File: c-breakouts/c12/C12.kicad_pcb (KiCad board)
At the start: 2 copper layers, 38.1 x 48.3 mm, 54 parts, among them J1 Conn_01x10_Female, J10 Conn_01x01_Male, J11 Conn_01x01_Male, J2 Conn_01x10_Female, J3 Conn_01x10_Female, J4 Conn_01x10_Female, J5 Conn_01x10_Female, J6 Conn_01x10_Female

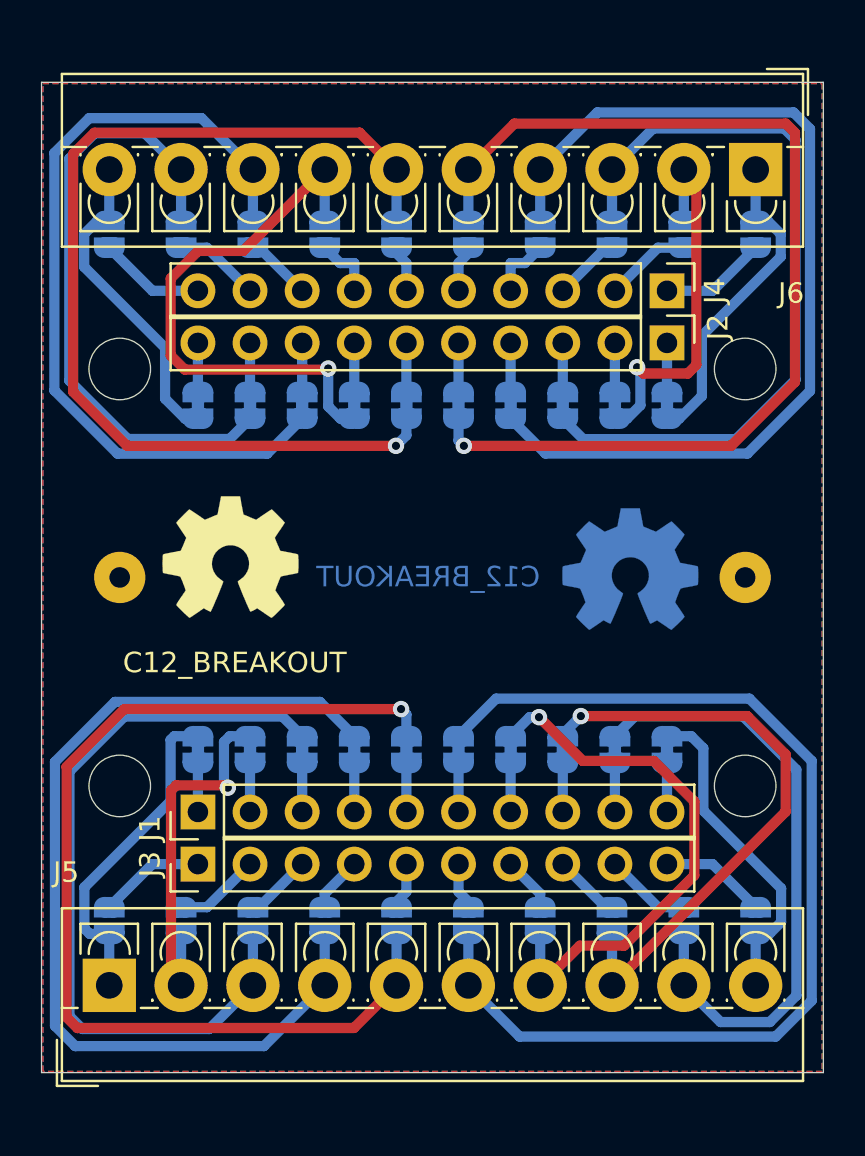
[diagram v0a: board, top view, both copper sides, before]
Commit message: fixed C12 connector position
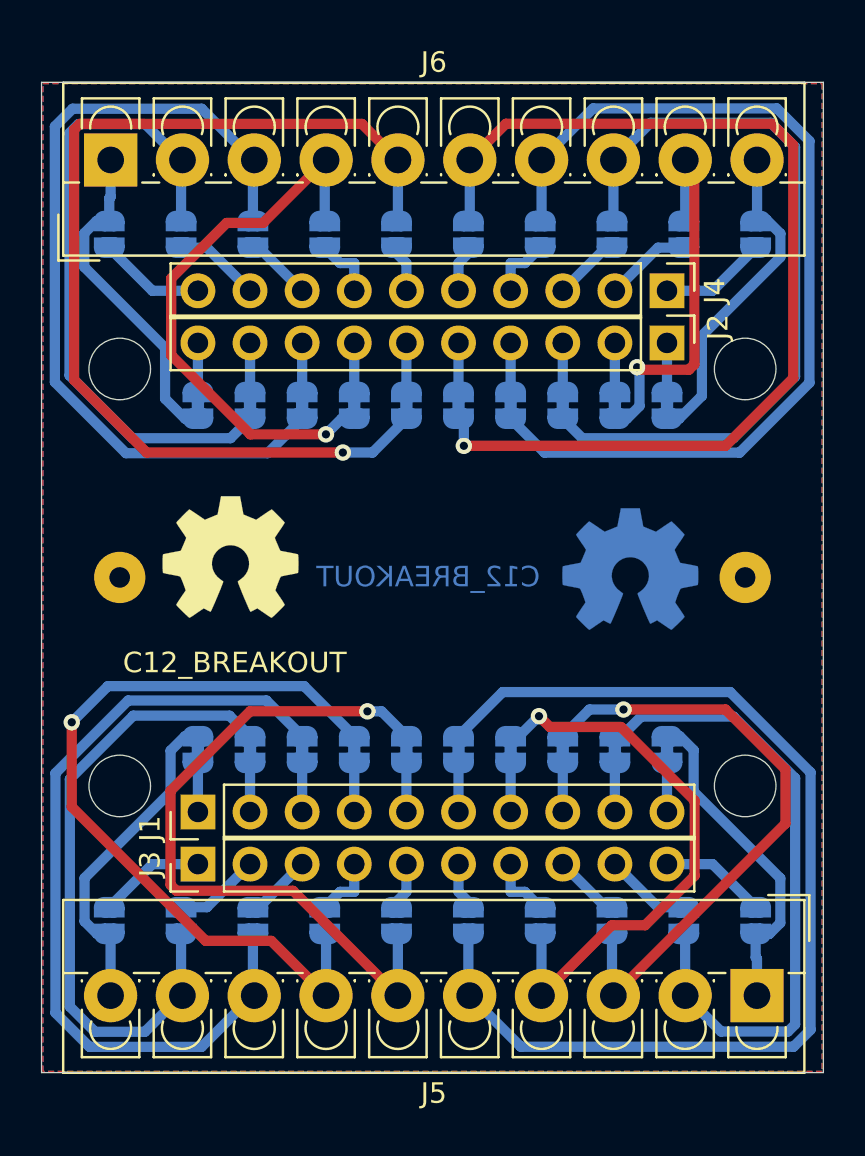
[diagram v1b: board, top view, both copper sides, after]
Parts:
- moved J5 31.6 mm to (54.9, 64.5), turned to 180 degrees
- moved J6 31.4 mm to (23.4, 23.8), turned to 0 degrees
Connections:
- J5 pad 1: Net-(J5-Pad1) -> Net-(JP10-Pad1)
- J5 pad 10: Net-(J5-Pad10) -> Net-(JP1-Pad1)
- J5 pad 2: Net-(J5-Pad2) -> Net-(JP19-Pad1)
- J5 pad 3: Net-(J5-Pad3) -> Net-(JP18-Pad1)
- J5 pad 4: Net-(J5-Pad4) -> Net-(JP17-Pad1)
- J5 pad 5: Net-(J5-Pad5) -> Net-(JP16-Pad1)
- J5 pad 6: Net-(J5-Pad6) -> Net-(JP15-Pad1)
- J5 pad 7: Net-(J5-Pad7) -> Net-(JP14-Pad1)
- J5 pad 8: Net-(J5-Pad8) -> Net-(JP13-Pad1)
- J5 pad 9: Net-(J5-Pad9) -> Net-(JP12-Pad1)
- J6 pad 1: Net-(J6-Pad1) -> Net-(JP30-Pad2)
- J6 pad 10: Net-(J6-Pad10) -> Net-(JP21-Pad2)
- J6 pad 2: Net-(J6-Pad2) -> Net-(JP29-Pad2)
- J6 pad 3: Net-(J6-Pad3) -> Net-(JP28-Pad2)
- J6 pad 4: Net-(J6-Pad4) -> Net-(JP27-Pad2)
- J6 pad 5: Net-(J6-Pad5) -> Net-(JP26-Pad2)
- J6 pad 6: Net-(J6-Pad6) -> Net-(JP25-Pad2)
- J6 pad 7: Net-(J6-Pad7) -> Net-(JP24-Pad2)
- J6 pad 8: Net-(J6-Pad8) -> Net-(JP23-Pad2)
- J6 pad 9: Net-(J6-Pad9) -> Net-(JP22-Pad2)
- JP1 pad 1: Net-(J5-Pad1) -> Net-(JP1-Pad1)
- JP10 pad 1: Net-(J5-Pad10) -> Net-(JP10-Pad1)
- JP11 pad 1: Net-(J5-Pad1) -> Net-(JP1-Pad1)
- JP12 pad 1: Net-(J5-Pad2) -> Net-(JP12-Pad1)
- JP13 pad 1: Net-(J5-Pad3) -> Net-(JP13-Pad1)
- JP14 pad 1: Net-(J5-Pad4) -> Net-(JP14-Pad1)
- JP15 pad 1: Net-(J5-Pad5) -> Net-(JP15-Pad1)
- JP16 pad 1: Net-(J5-Pad6) -> Net-(JP16-Pad1)
- JP17 pad 1: Net-(J5-Pad7) -> Net-(JP17-Pad1)
- JP18 pad 1: Net-(J5-Pad8) -> Net-(JP18-Pad1)
- JP19 pad 1: Net-(J5-Pad9) -> Net-(JP19-Pad1)
- JP2 pad 1: Net-(J5-Pad2) -> Net-(JP12-Pad1)
- JP20 pad 1: Net-(J5-Pad10) -> Net-(JP10-Pad1)
- JP21 pad 2: Net-(J6-Pad1) -> Net-(JP21-Pad2)
- JP22 pad 2: Net-(J6-Pad2) -> Net-(JP22-Pad2)
- JP23 pad 2: Net-(J6-Pad3) -> Net-(JP23-Pad2)
- JP24 pad 2: Net-(J6-Pad4) -> Net-(JP24-Pad2)
- JP25 pad 2: Net-(J6-Pad5) -> Net-(JP25-Pad2)
- JP26 pad 2: Net-(J6-Pad6) -> Net-(JP26-Pad2)
- JP27 pad 2: Net-(J6-Pad7) -> Net-(JP27-Pad2)
- JP28 pad 2: Net-(J6-Pad8) -> Net-(JP28-Pad2)
- JP29 pad 2: Net-(J6-Pad9) -> Net-(JP29-Pad2)
- JP3 pad 1: Net-(J5-Pad3) -> Net-(JP13-Pad1)
- JP30 pad 2: Net-(J6-Pad10) -> Net-(JP30-Pad2)
- JP31 pad 2: Net-(J6-Pad1) -> Net-(JP21-Pad2)
- JP32 pad 2: Net-(J6-Pad2) -> Net-(JP22-Pad2)
- JP33 pad 2: Net-(J6-Pad3) -> Net-(JP23-Pad2)
- JP34 pad 2: Net-(J6-Pad4) -> Net-(JP24-Pad2)
- JP35 pad 2: Net-(J6-Pad5) -> Net-(JP25-Pad2)
- JP36 pad 2: Net-(J6-Pad6) -> Net-(JP26-Pad2)
- JP37 pad 2: Net-(J6-Pad7) -> Net-(JP27-Pad2)
- JP38 pad 2: Net-(J6-Pad8) -> Net-(JP28-Pad2)
- JP39 pad 2: Net-(J6-Pad9) -> Net-(JP29-Pad2)
- JP4 pad 1: Net-(J5-Pad4) -> Net-(JP14-Pad1)
- JP40 pad 2: Net-(J6-Pad10) -> Net-(JP30-Pad2)
- JP5 pad 1: Net-(J5-Pad5) -> Net-(JP15-Pad1)
- JP6 pad 1: Net-(J5-Pad6) -> Net-(JP16-Pad1)
- JP7 pad 1: Net-(J5-Pad7) -> Net-(JP17-Pad1)
- JP8 pad 1: Net-(J5-Pad8) -> Net-(JP18-Pad1)
- JP9 pad 1: Net-(J5-Pad9) -> Net-(JP19-Pad1)
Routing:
- net Net-(JP16-Pad1): track 0.00 -> 53.2 mm
- net Net-(J5-Pad6): track 51.9 -> 0.00 mm
- net Net-(J5-Pad5): track 50.8 -> 0.00 mm, vias 1 -> 0
- net Net-(J6-Pad5): track 50.5 -> 0.00 mm, vias 1 -> 0
- net Net-(JP26-Pad2): track 0.00 -> 50.2 mm, vias 0 -> 1
- net Net-(JP25-Pad2): track 0.00 -> 50.1 mm, vias 0 -> 1
- net Net-(J6-Pad6): track 49.4 -> 0.00 mm, vias 1 -> 0
- net Net-(J5-Pad4): track 46.6 -> 0.00 mm
- net Net-(J6-Pad4): track 46.5 -> 0.00 mm
- net Net-(JP24-Pad2): track 0.00 -> 46.2 mm
- net Net-(JP28-Pad2): track 0.00 -> 40.7 mm
- net Net-(JP13-Pad1): track 0.00 -> 40.3 mm
- net Net-(J6-Pad8): track 39.6 -> 0.00 mm
- net Net-(JP14-Pad1): track 0.00 -> 38.9 mm, vias 0 -> 1
- net Net-(J5-Pad3): track 37.4 -> 0.00 mm
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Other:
- net class Default removed
- rule pad_to_mask_clearance: 0.051 -> 0
